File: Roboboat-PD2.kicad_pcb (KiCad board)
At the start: 2 copper layers, 78 x 60.7 mm, 48 parts, among them J1 14.4V, J10 Motor, J11 Motor, J12 Motor, J13 Motor, J14 Motor, J15 Motor, J16 Motor, J17 GND TP, J18 PGOOD TP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

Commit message: put SW1 on the correct side of the board
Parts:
- SW1: moved to F.Cu
- turned SW1 to -90 degrees
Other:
- board text removed: "SW1"

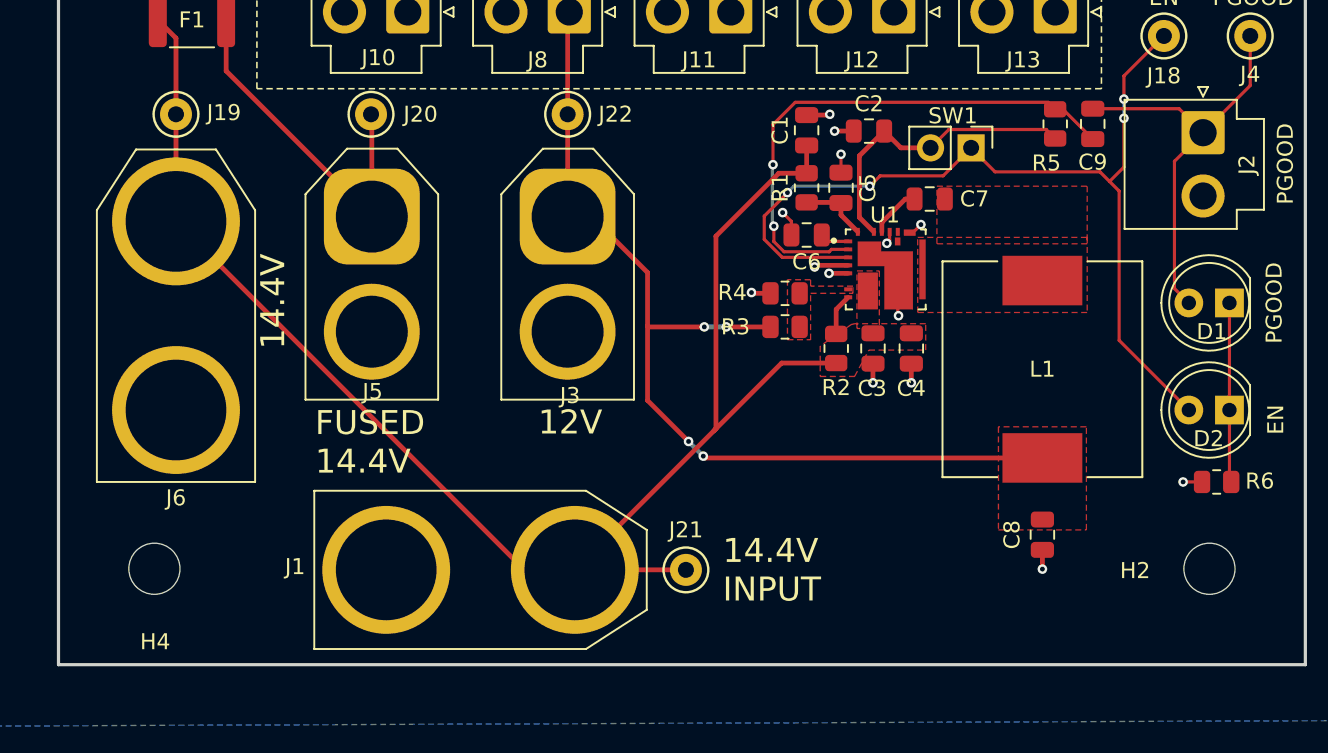
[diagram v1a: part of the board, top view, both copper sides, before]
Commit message: correct buck converter component values
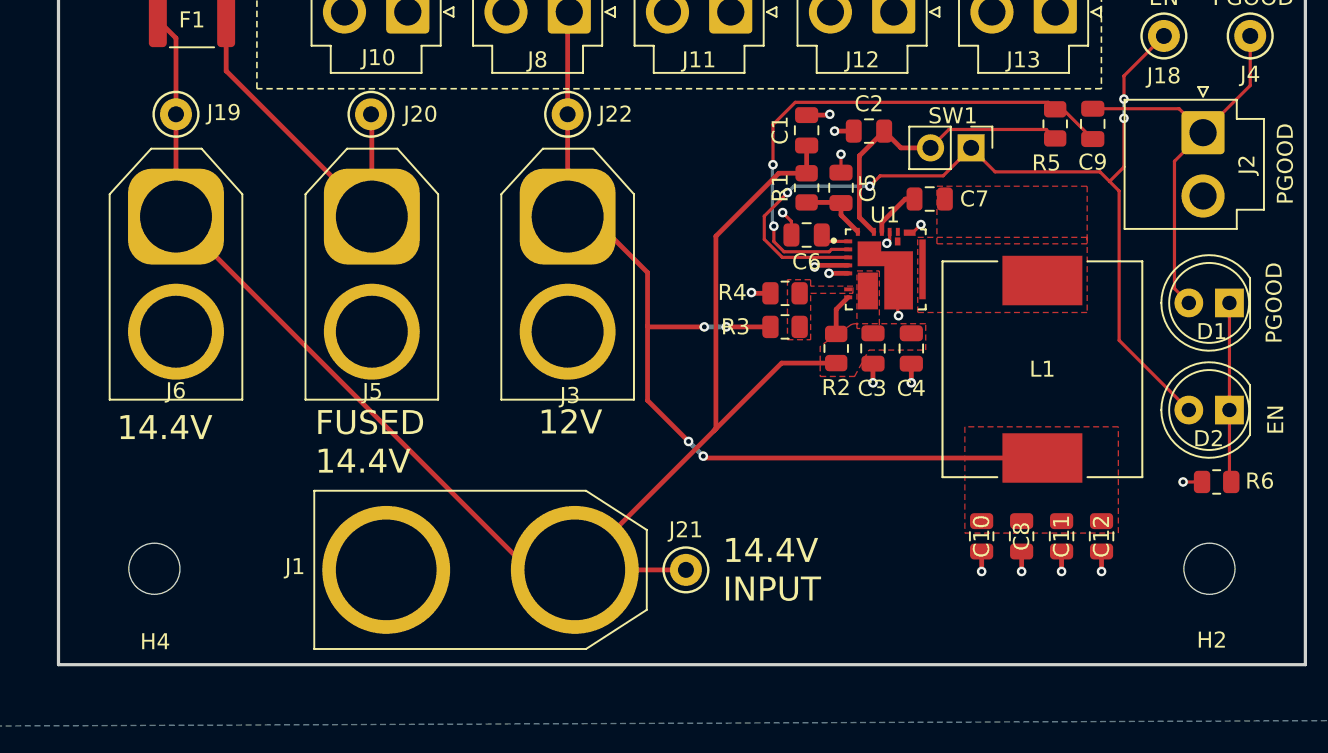
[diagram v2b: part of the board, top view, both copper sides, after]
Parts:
- added C10: 88uF, Capacitor_SMD:C_0805_2012Metric, F.Cu at (153.4, 135.3)
- added C11: 88uF, Capacitor_SMD:C_0805_2012Metric, F.Cu at (158.4, 135.3)
- added C12: 88uF, Capacitor_SMD:C_0805_2012Metric, F.Cu at (160.9, 135.3)
- C6: value 10nF -> 0.1uF
- C8: value 300uF -> 88uF
- J6: footprint footprints:XT90_V -> Connector_AMASS:AMASS_XT60-M_1x02_P7.20mm_Vertical
- L1: value 1uH -> 1.5uH
- R1: value 1.5uF -> 100k
- moved J6 6.20 mm to (103.0, 115.3), turned to -90 degrees
- moved C8 1.30 mm to (155.9, 135.3)
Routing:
- net GND: track 18.6 -> 22.4 mm, vias 14 -> 17
- net +14.4V: track 97.0 -> 99.0 mm

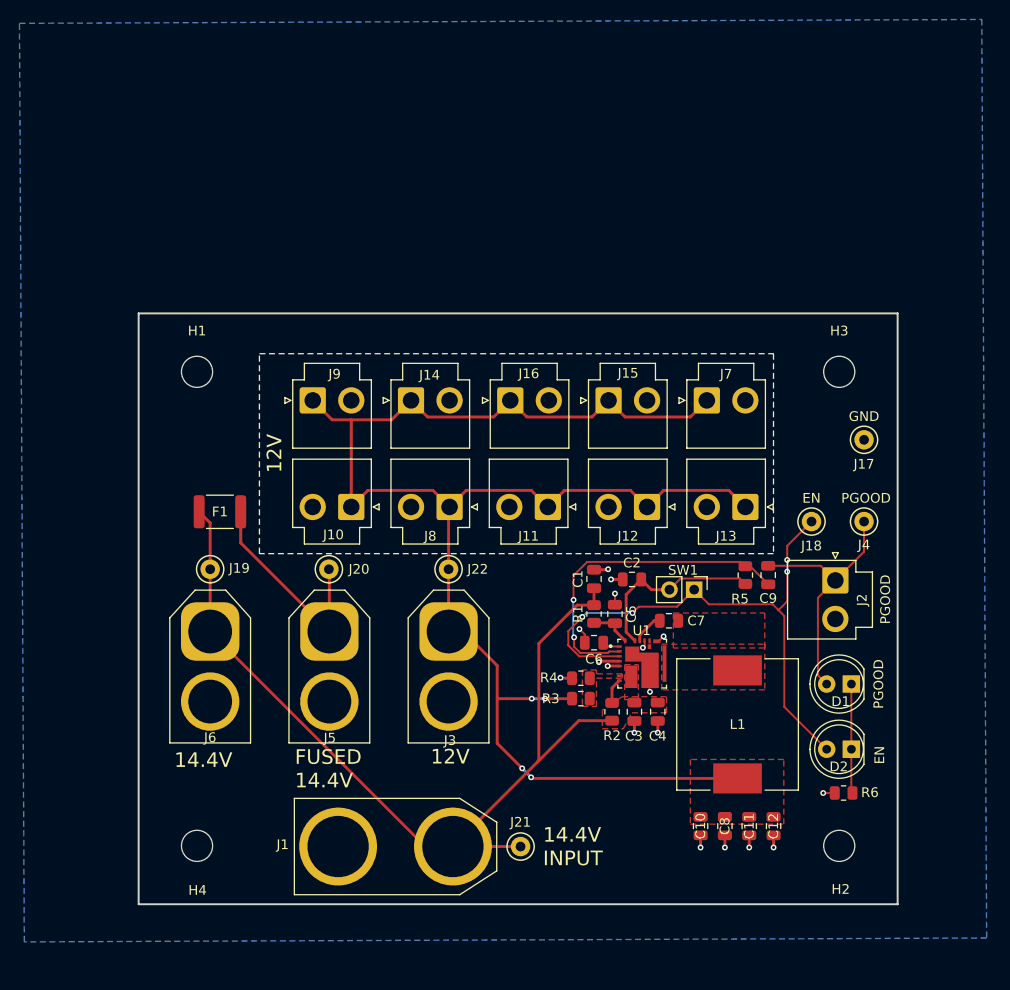
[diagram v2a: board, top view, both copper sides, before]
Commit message: make power traces thicker
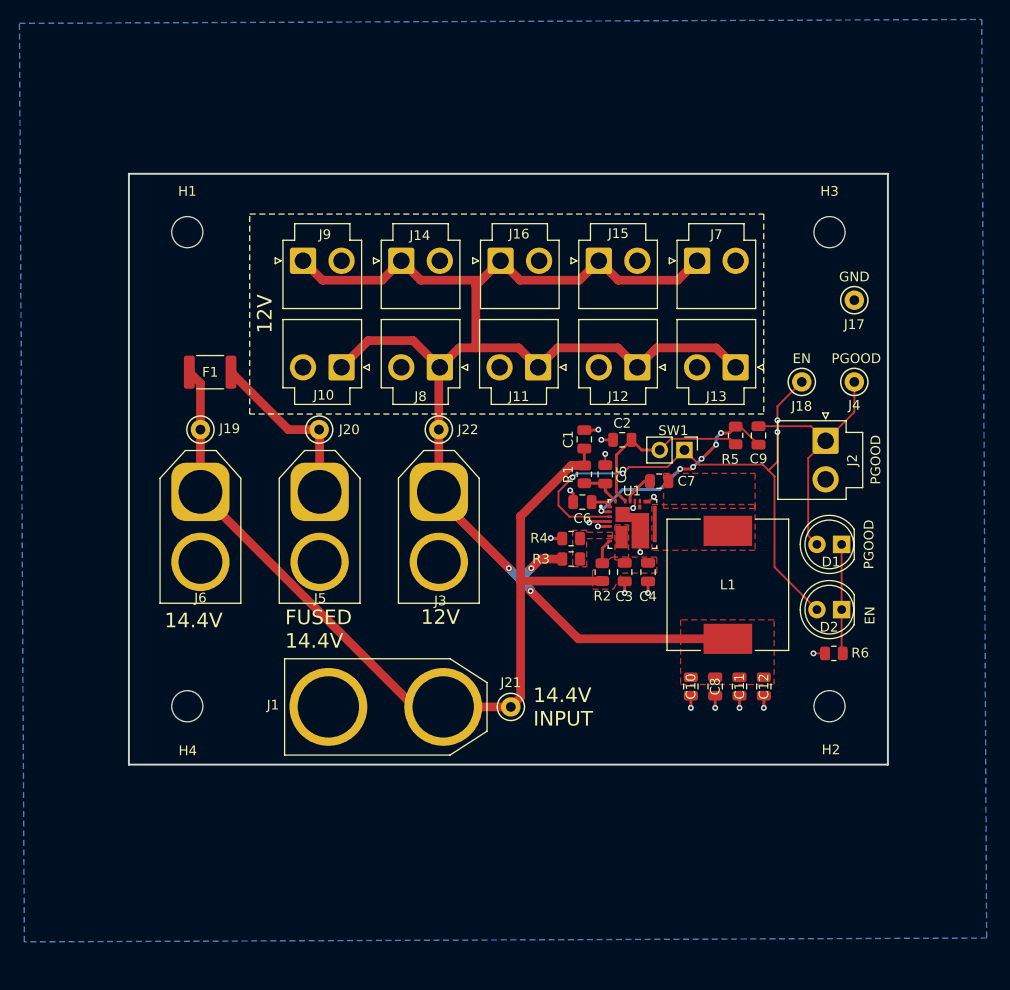
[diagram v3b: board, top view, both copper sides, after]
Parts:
- moved C6 14.5 mm to (141.2, 102.0)
- moved C1 14.4 mm to (141.4, 95.5)
- moved C10 14.4 mm to (152.4, 121.0)
- moved C11 14.4 mm to (157.4, 121.0)
- moved C12 14.4 mm to (159.9, 121.0)
- moved C2 14.4 mm to (145.3, 95.6)
- moved C7 14.4 mm to (149.2, 99.8)
- moved C8 14.4 mm to (154.9, 121.0)
- moved D1 14.4 mm to (167.9, 106.3)
- moved D2 14.4 mm to (167.9, 113.0)
- moved H2 14.4 mm to (166.7, 123.0)
- moved H4 14.4 mm to (100.7, 123.0)
- moved J1 14.4 mm to (121.0, 123.0)
- moved J19 14.4 mm to (102.0, 94.5)
- moved J20 14.4 mm to (114.2, 94.5)
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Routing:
- net Net-(U1-PGOOD): track 33.4 -> 21.3 mm, vias 2 -> 6
- net +14.4V: track 99.0 -> 89.7 mm
- net /14.4_F: track 22.5 -> 17.9 mm
- net +12V: track 163.3 -> 164.5 mm, vias 4 -> 3
- net Net-(U1-SS): track 1.25 -> 2.14 mm

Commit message: add GalaxSea logo
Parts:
- added G***: LOGO, LOGO, B.Cu at (102.9, 84.7)
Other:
- board text added: "12V Power Distribution Rev. 2 {dblquote}Frieren{dblquote}"
- board text removed: "GalaxSea 12V Power Distribution {dblquote}Frieren{dblquote} Rev. 2"

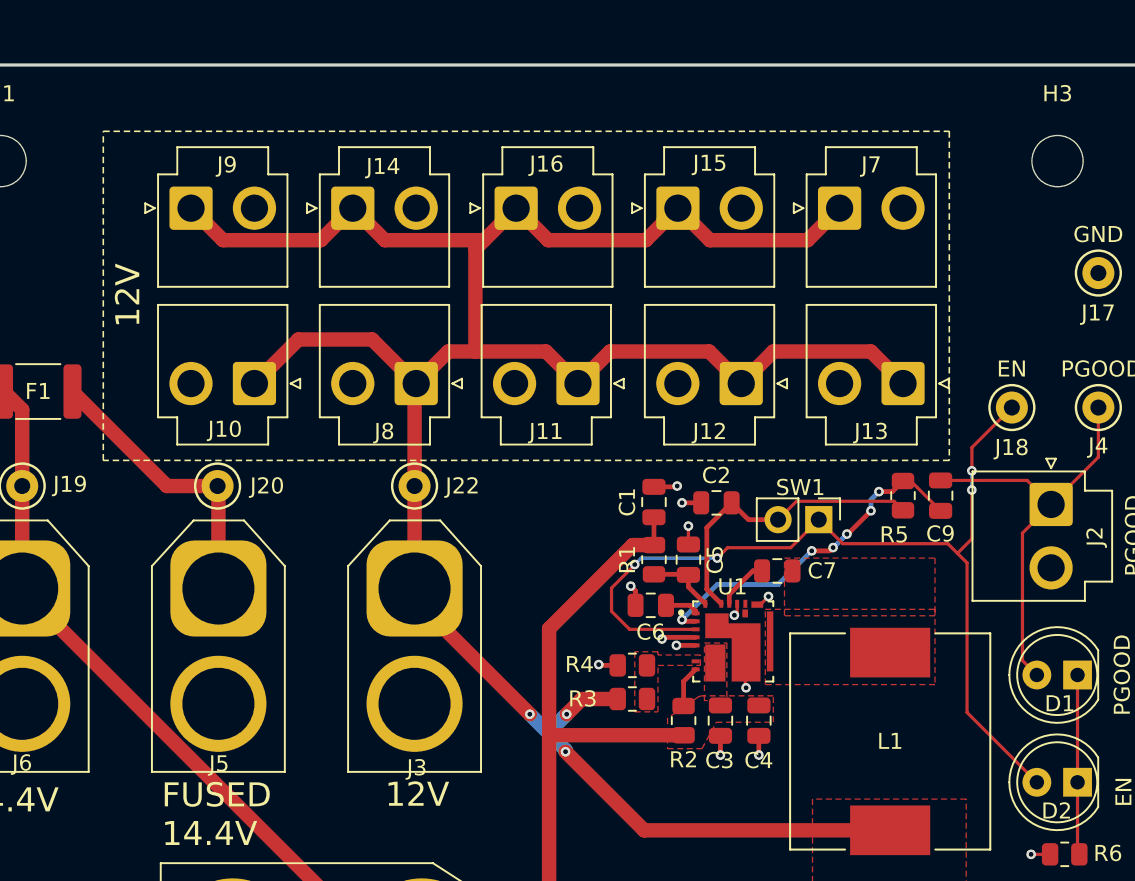
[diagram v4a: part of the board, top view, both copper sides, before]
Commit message: rotate SW1
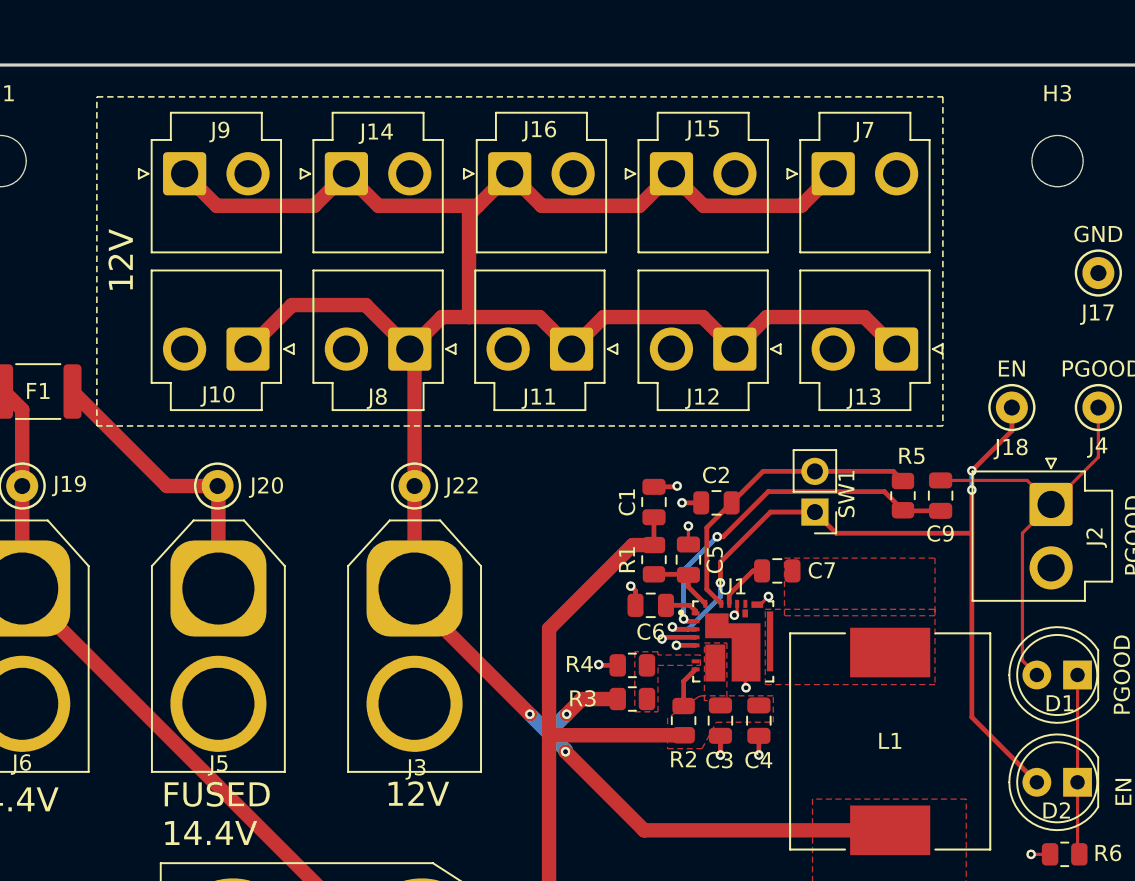
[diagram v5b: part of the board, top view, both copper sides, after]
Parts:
- moved J10 2.19 mm to (116.1, 86.0)
- moved J11 2.19 mm to (136.3, 86.0)
- moved J12 2.19 mm to (146.5, 86.0)
- moved J13 2.19 mm to (156.6, 86.0)
- moved J15 2.19 mm to (142.5, 75.0)
- moved J16 2.19 mm to (132.4, 75.0)
- moved J8 2.19 mm to (126.2, 86.0)
- moved J9 2.19 mm to (112.1, 75.0)
- moved J14 2.19 mm to (122.2, 75.0)
- moved J7 2.19 mm to (152.6, 75.0)
- moved SW1 0.53 mm to (151.5, 96.2), turned to 180 degrees
- turned R5 to -90 degrees
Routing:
- net +12V: track 164.5 -> 160.1 mm
- net /EN: track 58.3 -> 53.9 mm
- net Net-(U1-PGOOD): track 21.3 -> 22.4 mm, vias 6 -> 2

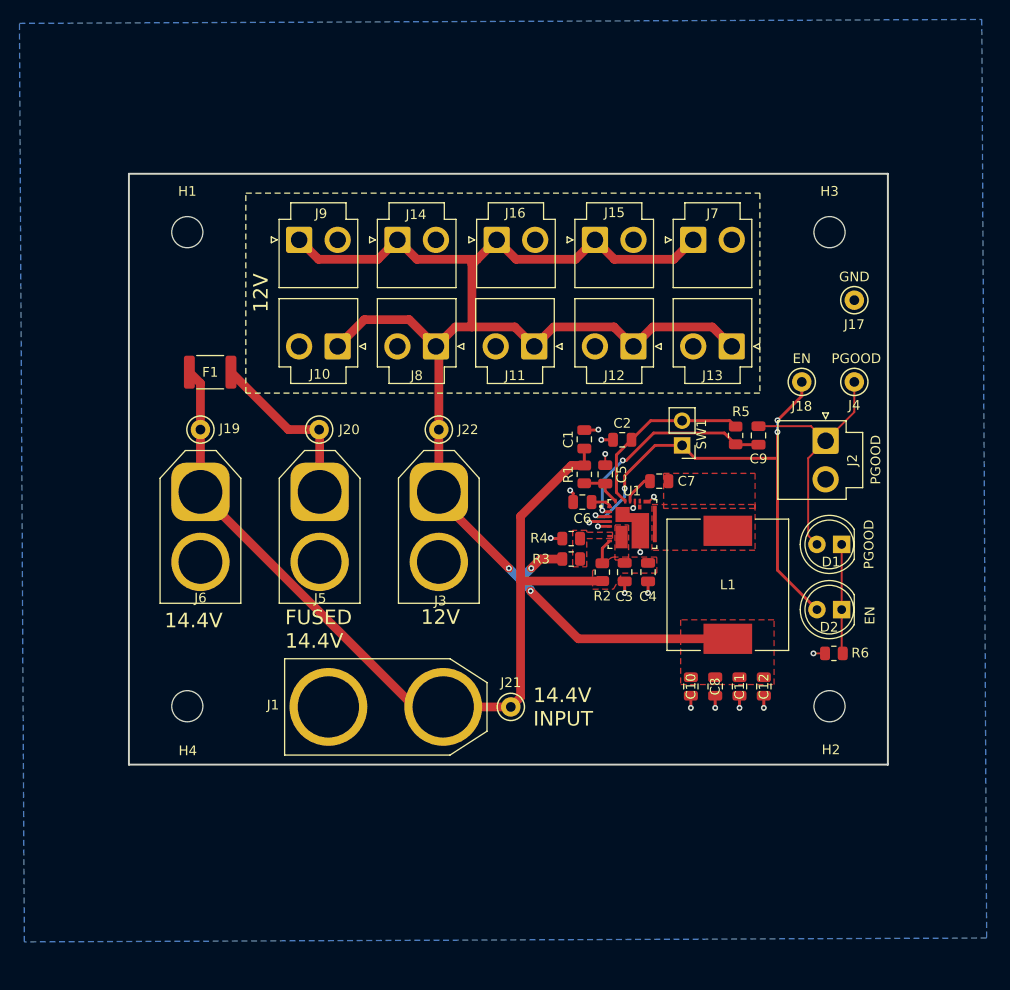
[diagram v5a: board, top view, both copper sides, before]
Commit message: move SW1
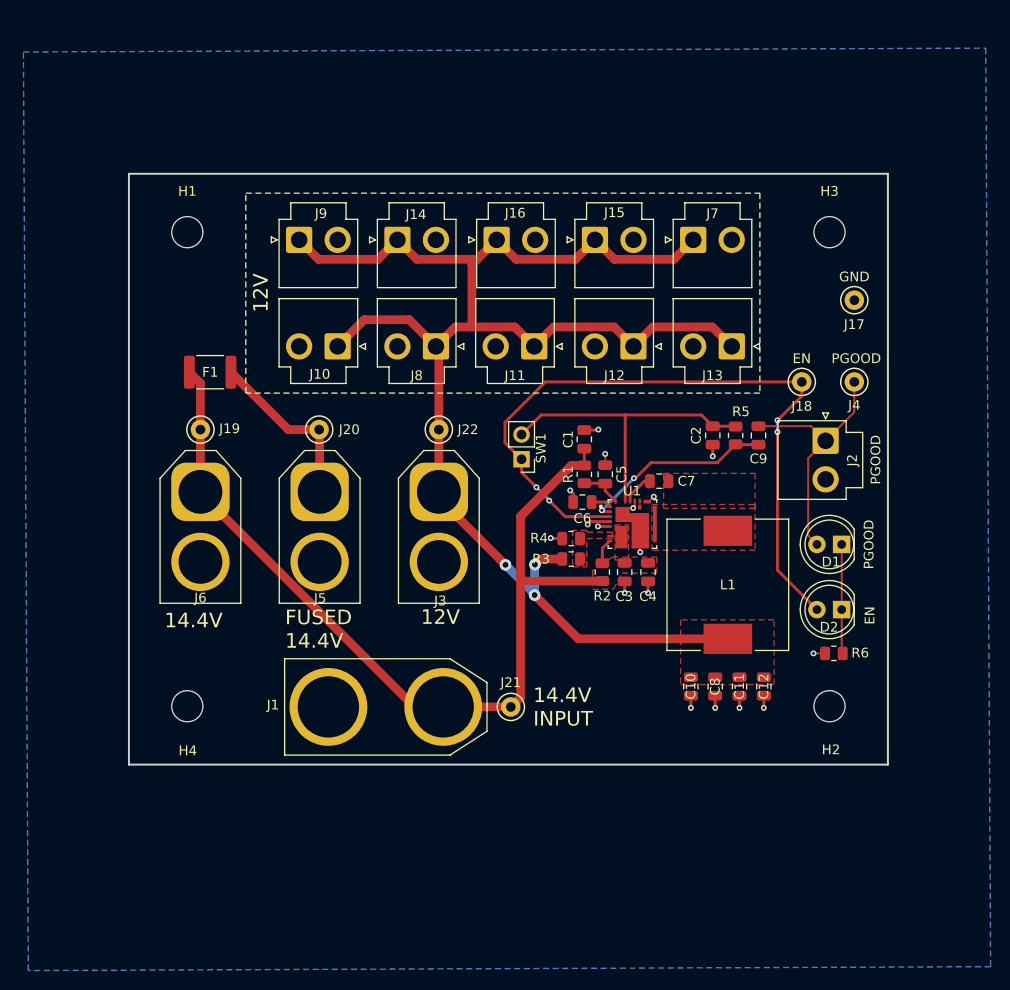
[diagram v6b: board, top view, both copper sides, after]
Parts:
- moved SW1 16.6 mm to (135.0, 97.6)
- moved C2 9.31 mm to (154.7, 95.2), turned to -90 degrees
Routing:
- net /EN: track 53.9 -> 75.2 mm
- net /VCC: track 19.1 -> 32.2 mm
- net Net-(U1-PGOOD): track 22.4 -> 19.9 mm
- net +12V: track 160.1 -> 162.4 mm
